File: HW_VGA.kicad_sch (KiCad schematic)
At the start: 2 parts, among them U1 25.175 MHz, U301 GAL22V10

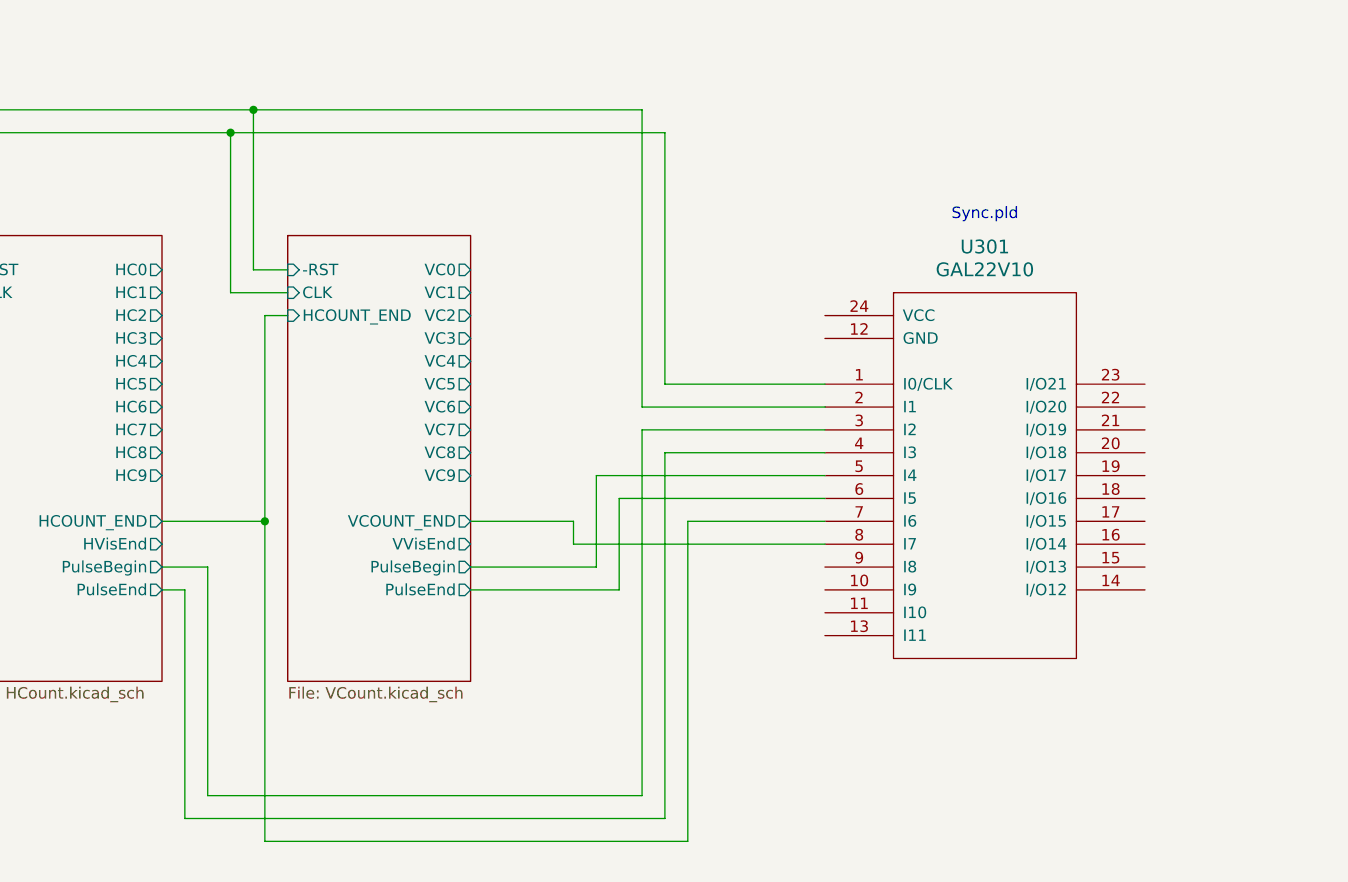
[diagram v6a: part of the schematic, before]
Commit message: use GAL22V10 for Sync module
Also, various improvements/cleanups to schematics.
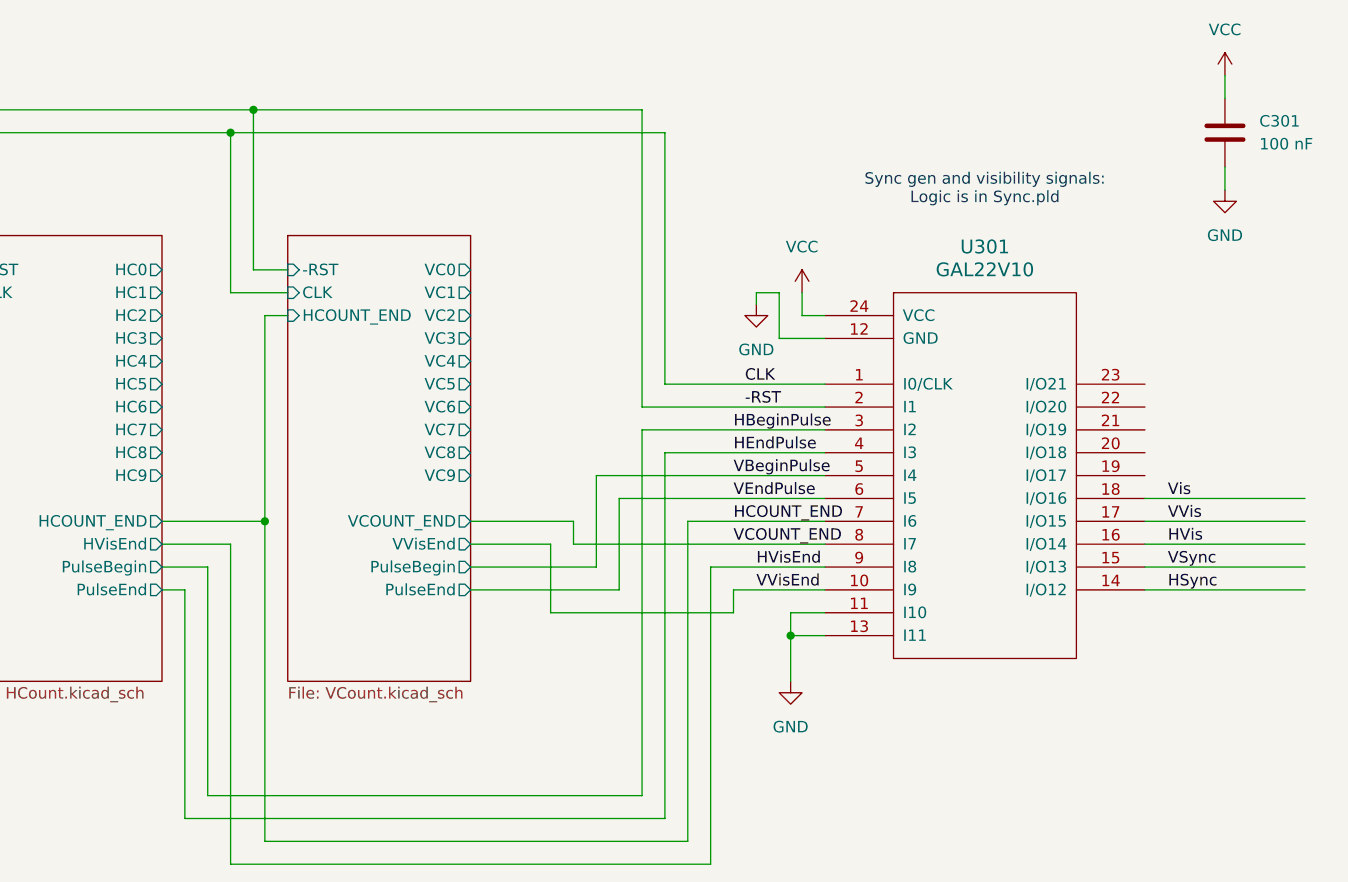
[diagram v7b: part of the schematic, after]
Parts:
- added C301: 100 nF, symbol Device:C
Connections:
- net GND: now also U301.11 (I10), U301.12 (GND), U301.13 (I11), C301.2
- net VCC: now also U301.24 (VCC), C301.1
- net VVisEnd: now reaches U301.10 (I9)
- net HSync: now reaches U301.14 (I/O12)
- net VSync: now reaches U301.15 (I/O13)
- net HVis: now reaches U301.16 (I/O14)
- net VVis: now reaches U301.17 (I/O15)
- net Vis: now reaches U301.18 (I/O16)
- net HVisEnd: now reaches U301.9 (I8)
- net HCount/-RST renamed -RST
- net HCount/CLK renamed CLK
- net HCount/HCOUNT_END renamed HCOUNT_END
- net HCount/PulseBegin renamed HBeginPulse
- net HCount/PulseEnd renamed HEndPulse
- net VCount/PulseBegin renamed VBeginPulse
- net VCount/PulseEnd renamed VEndPulse
- net VCount/VCOUNT_END renamed VCOUNT_END
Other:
- note added: "Sync gen and visibility signals: Logic is in Sync.pld"
- note removed: "Sync.pld"

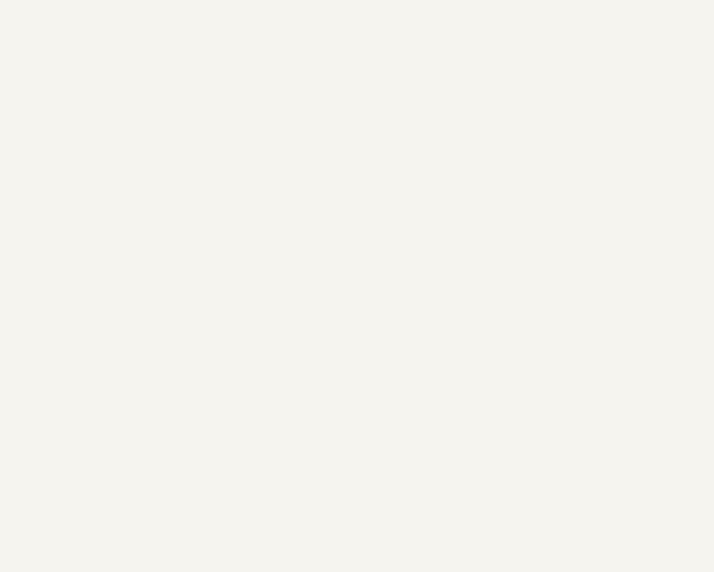
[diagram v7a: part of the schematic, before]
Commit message: added pixel output circuit
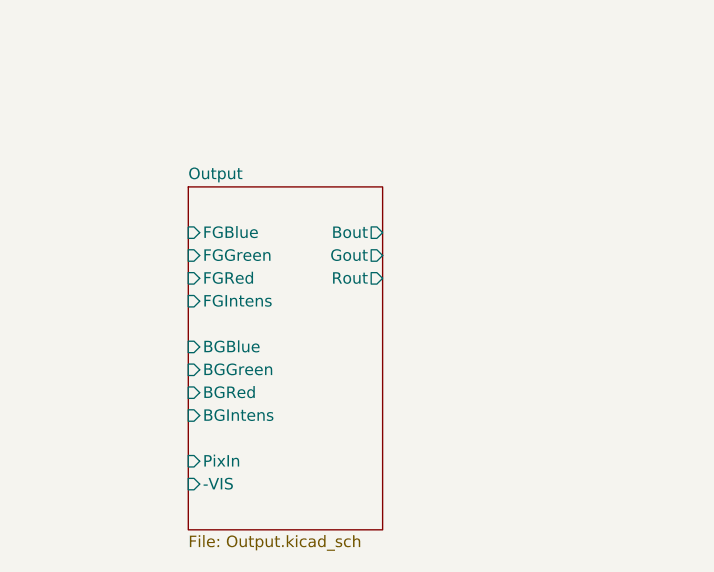
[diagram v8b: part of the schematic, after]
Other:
- added sheet Output (Output.kicad_sch)
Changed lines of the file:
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@@
+	)
+	(sheet
+		(at 38.1 148.59)
+		(size 21.59 38.1)
+		(fields_autoplaced yes)
+		(stroke
+			(width 0.1524)
+			(type solid)
+		)
+		(fill
+			(color 0 0 0 0.0000)
+		)
+		(property "Sheetname" "Output"
+			(at 38.1 147.8784 0)
+			(effects
+				(font
+					(size 1.27 1.27)
+				)
+				(justify left bottom)
+			)
+		)
+		(property "Sheetfile" "Output.kicad_sch"
+			(at 38.1 187.2746 0)
+			(effects
+				(font
+					(size 1.27 1.27)
+				)
+				(justify left top)
+			)
+		)
+		(pin "FGGreen" input
+			(at 38.1 156.21 180)
+			(effects
+				(font
+					(size 1.27 1.27)
+				)
+				(justify left)
+			)
+		)
+		(pin "FGIntens" input
+			(at 38.1 161.29 180)
+			(effects
+				(font
+					(size 1.27 1.27)
+				)
+				(justify left)
+			)
+		)
+		(pin "FGBlue" input
+			(at 38.1 153.67 180)
+			(effects
+				(font
+					(size 1.27 1.27)
+				)
+				(justify left)
+			)
+		)
+		(pin "FGRed" input
+			(at 38.1 158.75 180)
+			(effects
+				(font
+					(size 1.27 1.27)
+				)
+				(justify left)
+			)
+		)
+		(pin "PixIn" input
+			(at 38.1 179.07 180)
+			(effects
+				(font
+					(size 1.27 1.27)
+				)
+				(justify left)
+			)
+		)
+		(pin "-VIS" input
+			(at 38.1 181.61 180)
+			(effects
+				(font
+					(size 1.27 1.27)
+				)
+				(justify left)
+			)
+		)
+		(pin "BGRed" input
+			(at 38.1 171.45 180)
+			(effects
+				(font
+					(size 1.27 1.27)
+				)
+				(justify left)
+			)
+		)
+		(pin "BGBlue" input
+			(at 38.1 166.37 180)
+			(effects
+				(font
+					(size 1.27 1.27)
+				)
+				(justify left)
+			)
+		)
+		(pin "BGIntens" input
+			(at 38.1 173.99 180)
+			(effects
+				(font
+					(size 1.27 1.27)
+				)
+				(justify left)
+			)
+		)
+		(pin "BGGreen" input
+			(at 38.1 168.91 180)
+			(effects
+				(font
+					(size 1.27 1.27)
+				)
+				(justify left)
+			)
+		)
+		(pin "Bout" output
+			(at 59.69 153.67 0)
+			(effects
+				(font
+					(size 1.27 1.27)
+				)
+				(justify right)
+			)
+		)
+		(pin "Gout" output
+			(at 59.69 156.21 0)
+			(effects
+				(font
+					(size 1.27 1.27)
+				)
+				(justify right)
+			)
+		)
+		(pin "Rout" output
+			(at 59.69 158.75 0)
+			(effects
+				(font
+					(size 1.27 1.27)
+				)
+				(justify right)
+			)
+		)
+		(instances
+			(project "HW_VGA"
+				(path "/c4bd4b39-993a-4195-805f-b4de6fa4aea5"
+					(page "4")
+				)
+			)
+		)
 	)
 	(sheet
